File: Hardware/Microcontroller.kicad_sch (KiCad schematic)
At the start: 23 parts, among them J2 MICRO_SD, U1 XIAO-ESP32S3-PLUS

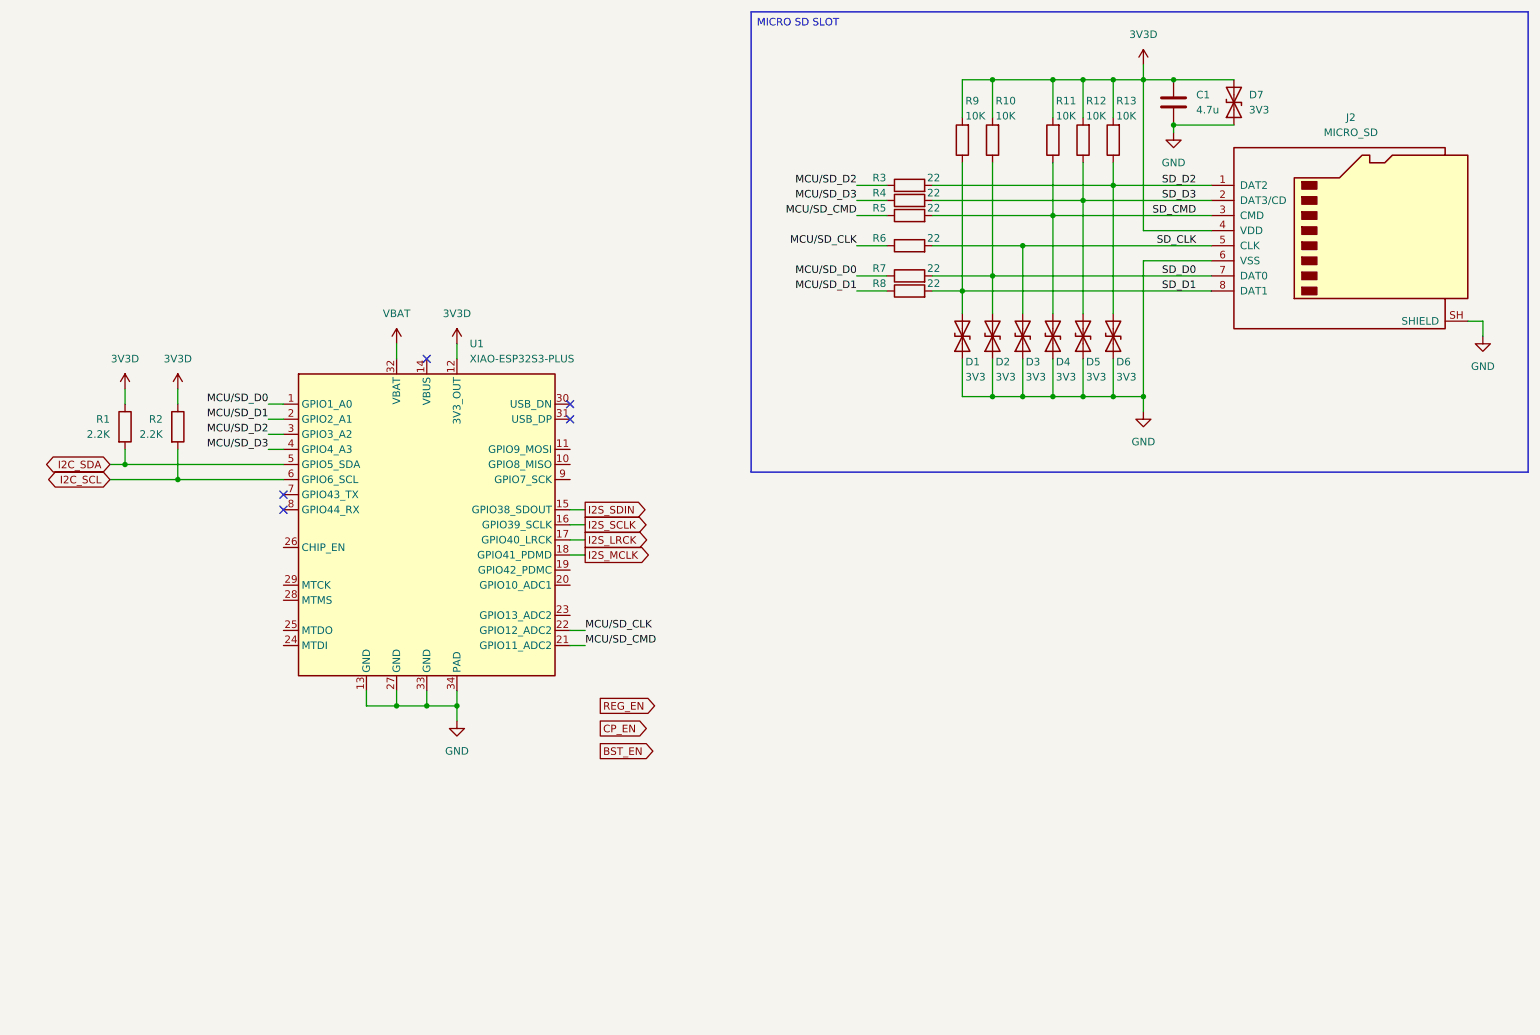
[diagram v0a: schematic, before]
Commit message: Expander and IO
Added an IO expander to the design.
Finished the main connections between the basic components.
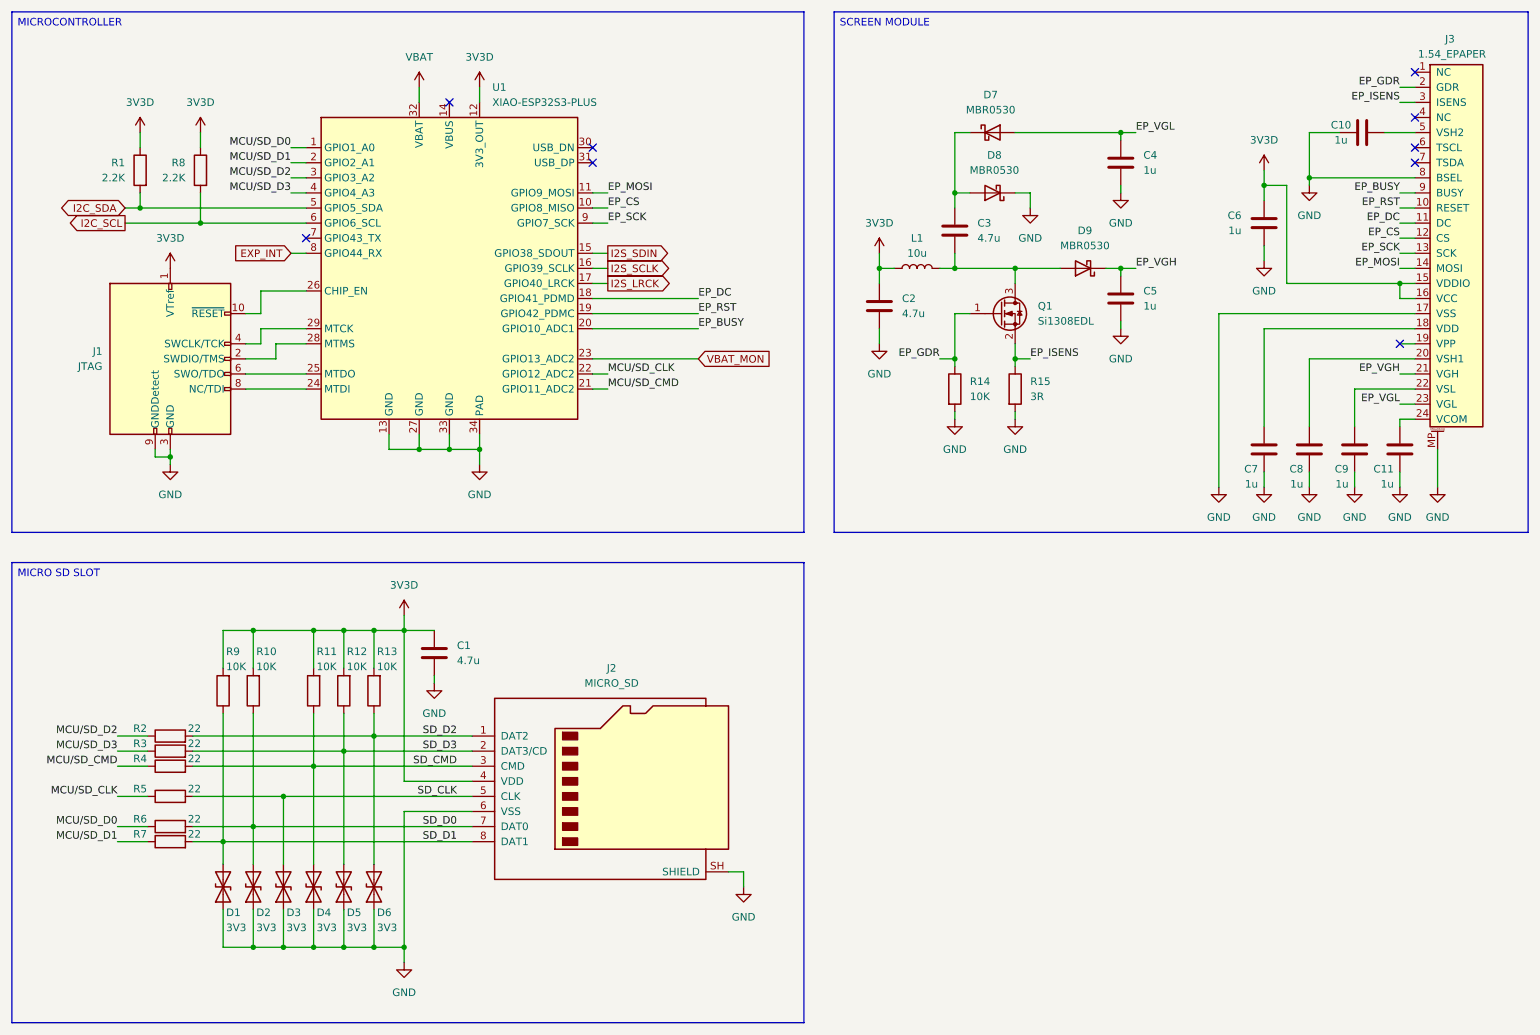
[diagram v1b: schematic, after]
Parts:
- removed D7: 3V3, symbol Device:D_TVS
- removed R2: 2.2K, symbol Device:R
- added C10, C11, C4, C5, C6, C7, C8, C9: 1u, Diode_SMD:D_SOD-123, symbol Device:C
- added C2, C3: 4.7u, Diode_SMD:D_SOD-123, symbol Device:C
- added D7, D8, D9: MBR0530, Diode_SMD:D_SOD-123, symbol Diode:MBR0530
- added J1: JTAG, Connector_PinHeader_1.27mm:PinHeader_2x05_P1.27mm_Vertical, symbol Connector:Conn_ARM_JTAG_SWD_10
- added J3: 1.54_EPAPER, RF_Module:ESP32-S3-WROOM-2, symbol Custom_Parts:WAVESHARE_1.54_EPAPER_MODULE
- added L1: 10u, Package_TO_SOT_SMD:SOT-323_SC-70, symbol Device:L
- added Q1: Si1308EDL, Package_TO_SOT_SMD:SOT-323_SC-70, symbol Transistor_FET:Si1308EDL
- added R14: 10K, symbol Device:R
- added R15: 3R, symbol Device:R
- added R8: 2.2K, symbol Device:R
- renumbered R3 to R2, R4 to R3, R5 to R4, R6 to R5, R7 to R6, R8 to R7
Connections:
- net 3V3D: now also C2.1, C6.1, J1.1 (VTref), J3.15 (VDDIO), J3.16 (VCC), L1.1, R8.1
- net GND: now also C10.1, C11.2, C2.2, C4.2, C5.2, C6.2, C7.2, C8.2, C9.2, D8.1 (K), J1.3 (GND), J1.5 (GND), J1.9 (GNDDetect), J3.17 (VSS), J3.8 (BSEL), J3.MP, R14.2, R15.2
- net I2C_SCL: now also R8.2
- net EP_CS: now reaches U1.10 (GPIO8_MISO)
- net EP_CS: now also J3.12 (CS)
- net EP_MOSI: now reaches U1.11 (GPIO9_MOSI)
- net EP_MOSI: now also J3.14 (MOSI)
- net EP_RST: now reaches U1.19 (GPIO42_PDMC)
- net EP_RST: now also J3.10 (RESET)
- net EP_BUSY: now reaches U1.20 (GPIO10_ADC1)
- net EP_BUSY: now also J3.9 (BUSY)
- net VBAT_MON: now reaches U1.23 (GPIO13_ADC2)
- net at U1.24 (MTDI): now also J1.8 (NC/TDI)
- net at U1.25 (MTDO): now also J1.6 (SWO/TDO)
- net at U1.26 (CHIP_EN): now also J1.10 (~{RESET})
- net at U1.28 (MTMS): now also J1.2 (SWDIO/TMS)
- net at U1.29 (MTCK): now also J1.4 (SWCLK/TCK)
- net EXP_INT: now reaches U1.8 (GPIO44_RX)
- net EP_SCK: now reaches U1.9 (GPIO7_SCK)
- net EP_SCK: now also J3.13 (SCK)
- net I2S_MCLK renamed EP_DC
- net EP_DC: now also J3.11 (DC)
- new net: C3.1, D7.1 (K), D8.2 (A)
- new net: C3.2, D9.2 (A), L1.2, Q1.3 (D)
- new net: C10.2, J3.5 (VSH2)
- new net: C11.1, J3.24 (VCOM)
- new net: C7.1, J3.18 (VDD)
- new net: C8.1, J3.20 (VSH1)
- new net: C9.1, J3.22 (VSL)
- new net EP_GDR: J3.2 (GDR), Q1.1 (G), R14.1
- new net EP_ISENS: J3.3 (ISENS), Q1.2 (S), R15.1
- new net EP_VGH: C5.1, D9.1 (K), J3.21 (VGH)
- new net EP_VGL: C4.1, D7.2 (A), J3.23 (VGL)
- no-connect marks 5 -> 9
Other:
- moved on the sheet: C1, D1, D2, D3, D4, D5, D6, J2, R10, R11, R12, R13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
